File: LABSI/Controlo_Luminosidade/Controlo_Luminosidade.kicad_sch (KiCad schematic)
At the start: 43 parts, among them J1 Barrel_Jack_Switch, J10 Conn_01x03_Socket, J2 Barrel_Jack_Switch, J3 Conn_01x05_Pin, J4 Conn_01x04_Pin, J5 Conn_01x04_Pin, J6 AVR-ISP-6, J7 Conn_01x03_Pin, J8 Conn_01x03_Pin, J9 Conn_01x05_Pin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

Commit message: micro standalone, bug it reading lux sensors
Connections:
- net +5V: now also R1.2; no longer J6.5 (~{RST}), R1.1, U1.1 (~{RESET}/PC6)
- net GND: no longer R1.2
- net INT_PCF: no longer U1.14 (PB0)
- net at J10.2 (Pin_2), R8.2: no longer U3.11 (P6)
- new net RST-AVR: J6.5 (~{RST}), R1.1, U1.1 (~{RESET}/PC6)
- no-connect marks 8 -> 10
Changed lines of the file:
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@@
 	)
 	(junction
-		(at 116.84 45.72)
-		(diameter 0)
-		(color 0 0 0 0)
-	)
-	(junction
 		(at 233.68 92.71)
 		(diameter 0)
@@
 		(color 0 0 0 0)
 	)
-	(junction
-		(at 247.65 31.75)
-		(diameter 0)
-		(color 0 0 0 0)
-	)
 	(no_connect
 		(at 194.31 142.24)
@@
 	)
 	(no_connect
+		(at 194.31 81.28)
+	)
+	(no_connect
 		(at 194.31 106.68)
 	)
 	(no_connect
+		(at 104.14 45.72)
+	)
+	(no_connect
 		(at 194.31 134.62)
 	)
@@
 	(wire
 		(pts
-			(xy 247.65 31.75) (xy 248.92 31.75)
-		)
-		(stroke
-			(width 0)
-			(type default)
-		)
-	)
-	(wire
-		(pts
-			(xy 104.14 45.72) (xy 116.84 45.72)
-		)
-		(stroke
-			(width 0)
-			(type default)
-		)
-	)
-	(wire
-		(pts
 			(xy 195.58 20.32) (xy 203.2 20.32)
 		)
@@
 		)
 	)
-	(label "INT_PCF"
-		(at 194.31 81.28 0)
-		(effects
-			(font
-				(size 1.27 1.27)
-			)
-			(justify left bottom)
-		)
-	)
 	(label "XTAL1"
 		(at 259.08 59.69 0)
@@
 	(symbol
 		(lib_id "power:+5V")
-		(at 248.92 31.75 270)
+		(at 247.65 40.64 180)
 		(unit 1)
 		(exclude_from_sim no)
@@
 		(dnp no)
 		(property "Reference" "#PWR06"
-			(at 245.11 31.75 0)
+			(at 247.65 36.83 0)
 			(effects
 				(font
@@
 		)
 		(property "Value" "+5V"
-			(at 252.476 30.48 0)
+			(at 248.92 44.196 0)
 			(effects
 				(font
@@
 		)
 		(property "Footprint" ""
-			(at 248.92 31.75 0)
+			(at 247.65 40.64 0)
 			(effects
 				(font
@@
 		)
 		(property "Datasheet" ""
-			(at 248.92 31.75 0)
+			(at 247.65 40.64 0)
 			(effects
 				(font
@@
 		)
 		(property "Description" "Power symbol creates a global label with name \"+5V\""
-			(at 248.92 31.75 0)
+			(at 247.65 40.64 0)
 			(effects
 				(font
@@
 					(unit 1)
 				)
-			)
-		)
-	)
-	(symbol
-		(lib_id "power:GND")
-		(at 247.65 40.64 0)
-		(unit 1)
-		(exclude_from_sim no)
-		(in_bom yes)
-		(on_board yes)
-		(dnp no)
-		(property "Reference" "#PWR08"
-			(at 247.65 46.99 0)
-			(effects
-				(font
-					(size 1.27 1.27)
-				)
-				(hide yes)
-			)
-		)
-		(property "Value" "GND"
-			(at 246.126 44.196 0)
-			(effects
-				(font
-					(size 1.27 1.27)
-				)
-			)
-		)
-		(property "Footprint" ""
-			(at 247.65 40.64 0)
-			(effects
-				(font
-					(size 1.27 1.27)
-				)
-				(hide yes)
-			)
-		)
-		(property "Datasheet" ""
-			(at 247.65 40.64 0)
-			(effects
-				(font
-					(size 1.27 1.27)
-				)
-				(hide yes)
-			)
-		)
-		(property "Description" "Power symbol creates a global label with name \"GND\" , ground"
-			(at 247.65 40.64 0)
-			(effects
-				(font
-					(size 1.27 1.27)
-				)
-				(hide yes)
-			)
-		)
-		(pin "1"
-		)
-		(instances
-			(project "Controlo_Luminosidade"
-				(path "/fe63ea70-5567-4436-89bb-13eb6300ee5a"
-					(reference "#PWR08")
-					(unit 1)
-				)

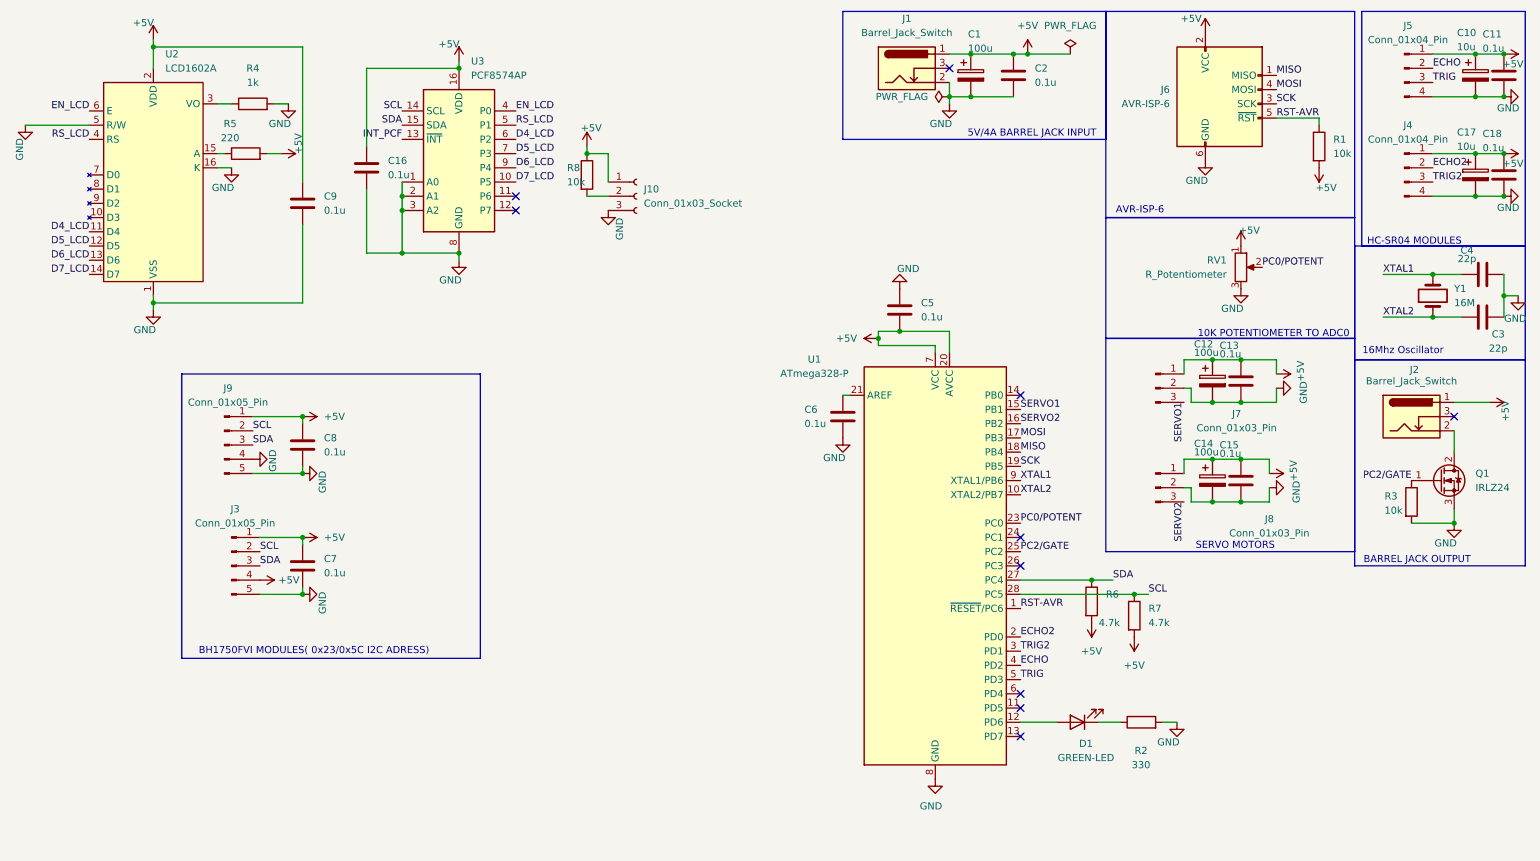
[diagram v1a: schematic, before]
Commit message: rotina maquina de estados inic; i2c, 2 sensors bug fixed, button logic added
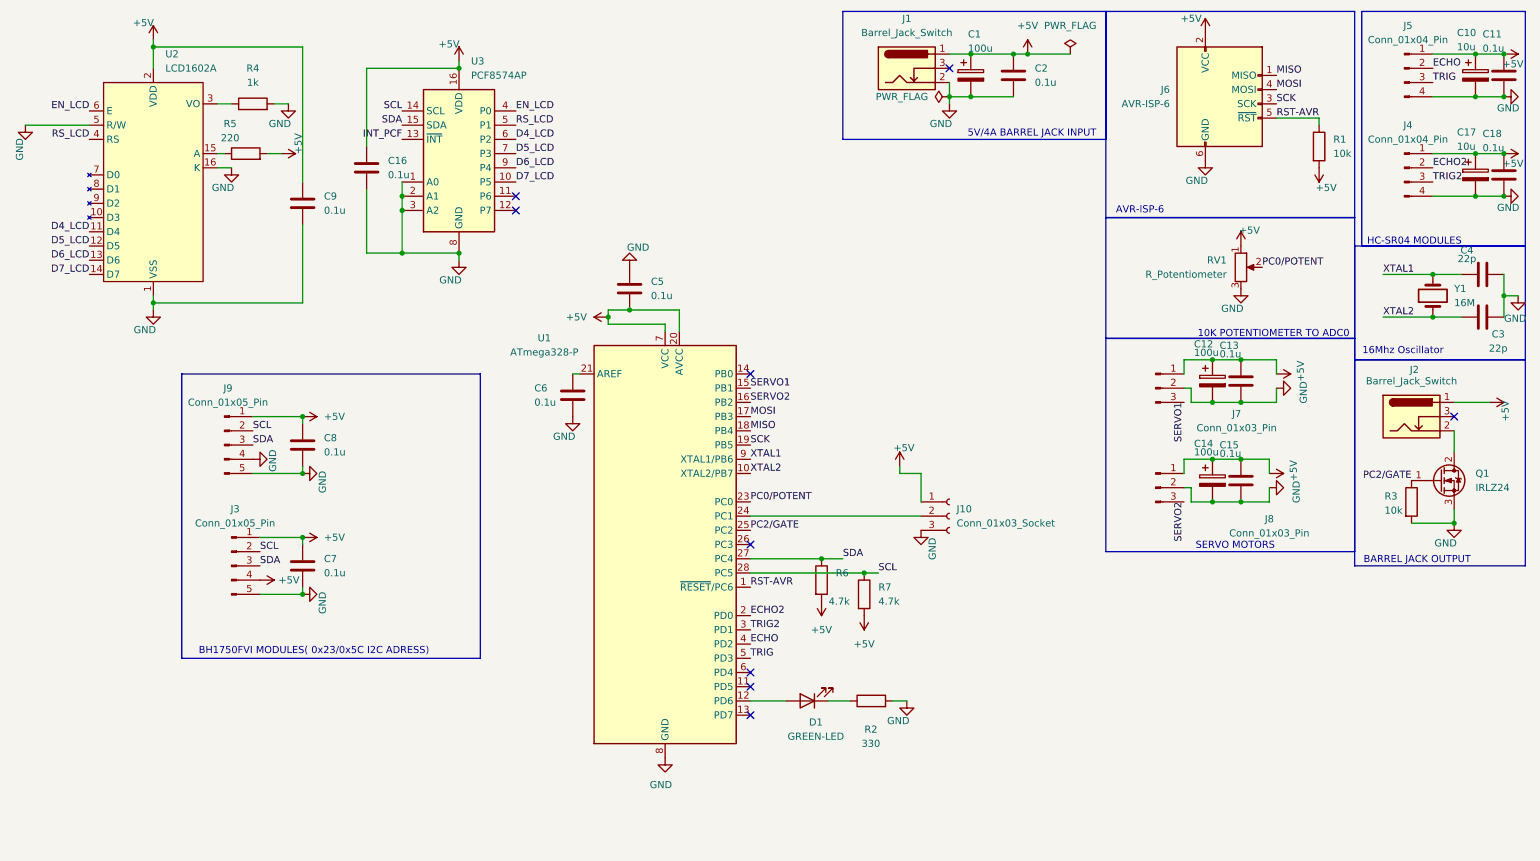
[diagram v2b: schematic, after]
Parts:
- removed R8: 10k, symbol Device:R
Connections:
- net at J10.2 (Pin_2): now also U1.24 (PC1)
- no-connect marks 10 -> 9
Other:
- moved on the sheet: C5, C6, D1, J10, R2, R6, R7, U1

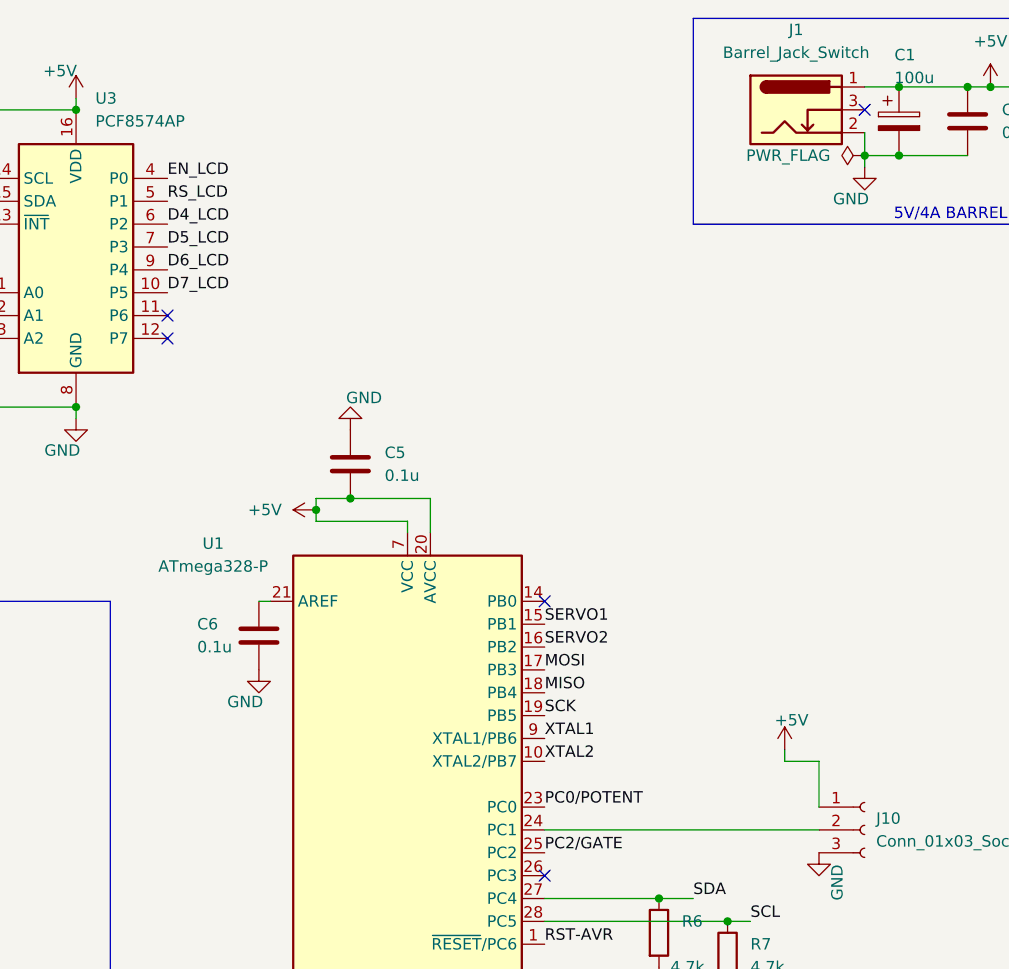
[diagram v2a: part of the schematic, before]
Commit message: maquina estados controlo adc, butao para modos, mapeamento para saltos de 50 e fixação setpoint
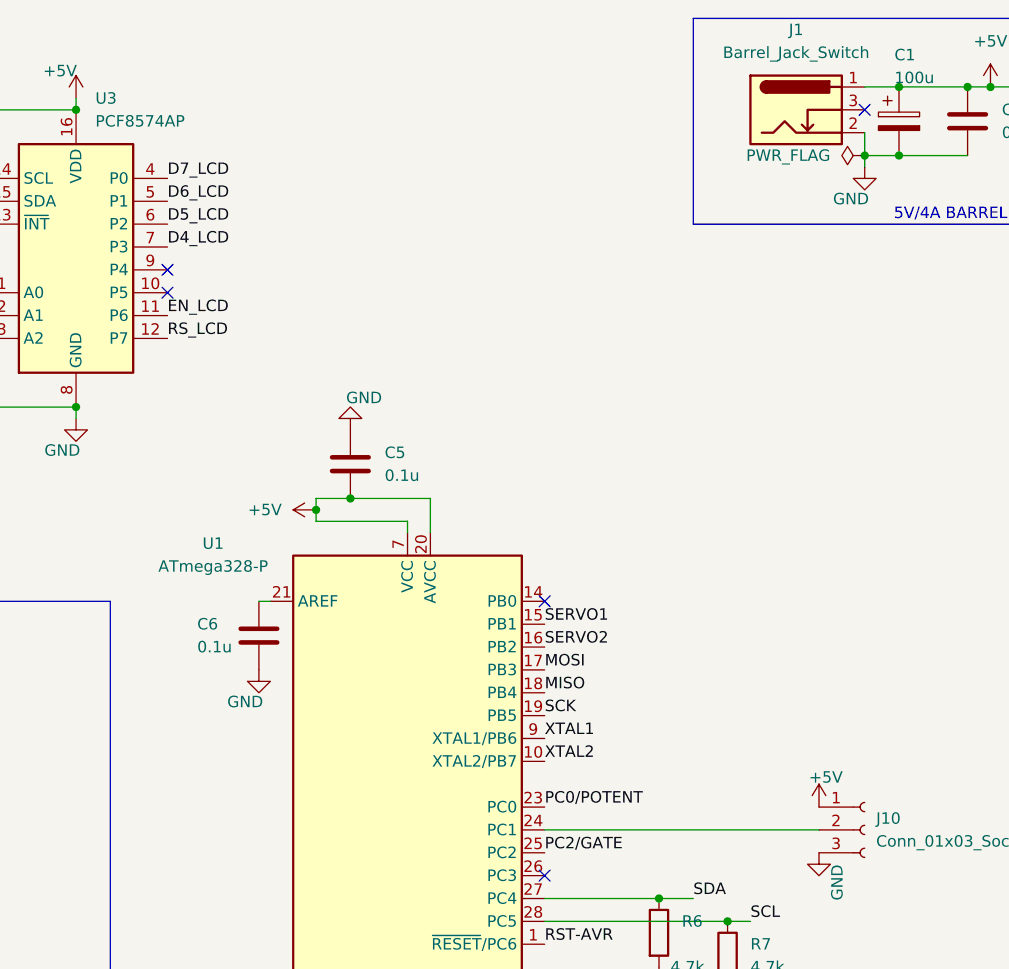
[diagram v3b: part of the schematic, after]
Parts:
- J10: footprint (none) -> Connector_PinSocket_2.54mm:PinSocket_1x03_P2.54mm_Vertical
- R6, R7: footprint (none) -> Resistor_THT:R_Axial_DIN0204_L3.6mm_D1.6mm_P5.08mm_Horizontal
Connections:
- net D4_LCD: now also U3.7 (P3); no longer U3.6 (P2)
- net D5_LCD: now also U3.6 (P2); no longer U3.7 (P3)
- net D6_LCD: now also U3.5 (P1); no longer U3.9 (P4)
- net D7_LCD: now also U3.4 (P0); no longer U3.10 (P5)
- net EN_LCD: now also U3.11 (P6); no longer U3.4 (P0)
- net RS_LCD: now also U3.12 (P7); no longer U3.5 (P1)
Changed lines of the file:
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@@
 	)
 	(no_connect
+		(at 104.14 40.64)
+	)
+	(no_connect
 		(at 146.05 138.43)
 	)
@@
 	)
 	(no_connect
-		(at 104.14 45.72)
+		(at 104.14 43.18)
 	)
 	(no_connect
@@
 	)
 	(no_connect
-		(at 104.14 48.26)
-	)
-	(no_connect
 		(at 146.05 107.95)
 	)
@@
 	(wire
 		(pts
-			(xy 172.72 95.25) (xy 176.53 95.25)
-		)
-		(stroke
-			(width 0)
-			(type default)
-		)
-	)
-	(wire
-		(pts
 			(xy 280.67 38.1) (xy 275.59 38.1)
 		)
@@
 	(wire
 		(pts
-			(xy 172.72 93.98) (xy 172.72 95.25)
-		)
-		(stroke
-			(width 0)
-			(type default)
-		)
-	)
-	(wire
-		(pts
 			(xy 224.79 82.55) (xy 228.6 82.55)
 		)
@@
 	(wire
 		(pts
-			(xy 176.53 95.25) (xy 176.53 100.33)
-		)
-		(stroke
-			(width 0)
-			(type default)
-		)
-	)
-	(wire
-		(pts
 			(xy 185.42 27.94) (xy 193.04 27.94)
 		)
@@
 	)
 	(label "D7_LCD"
-		(at 104.14 43.18 0)
+		(at 104.14 30.48 0)
 		(effects
 			(font
@@
 	)
 	(label "EN_LCD"
-		(at 104.14 30.48 0)
+		(at 104.14 45.72 0)
 		(effects
 			(font
@@
 	)
 	(label "D4_LCD"
-		(at 104.14 35.56 0)
+		(at 104.14 38.1 0)
 		(effects
 			(font
@@
 	)
 	(label "D5_LCD"
-		(at 104.14 38.1 0)
+		(at 104.14 35.56 0)
 		(effects
 			(font
@@
 	)
 	(label "D6_LCD"
-		(at 104.14 40.64 0)
+		(at 104.14 33.02 0)
 		(effects
 			(font
@@
 	)
 	(label "RS_LCD"
-		(at 104.14 33.02 0)
+		(at 104.14 48.26 0)
 		(effects
 			(font
@@
 			)
 		)
-		(property "Footprint" ""
+		(property "Footprint" "Resistor_THT:R_Axial_DIN0204_L3.6mm_D1.6mm_P5.08mm_Horizontal"
 			(at 156.972 114.3 90)
 			(effects
@@
 			)
 		)
-		(property "Footprint" ""
+		(property "Footprint" "Connector_PinSocket_2.54mm:PinSocket_1x03_P2.54mm_Vertical"
 			(at 181.61 102.87 0)
 			(effects
@@
 			)
 		)
-		(property "Footprint" ""
+		(property "Footprint" "Resistor_THT:R_Axial_DIN0204_L3.6mm_D1.6mm_P5.08mm_Horizontal"
 			(at 164.592 116.84 90)
 			(effects
@@
 	(symbol
 		(lib_id "power:+5V")
-		(at 172.72 93.98 0)
+		(at 176.53 100.33 0)
 		(unit 1)
 		(exclude_from_sim no)
@@
 		(dnp no)
 		(property "Reference" "#PWR042"
-			(at 172.72 97.79 0)
+			(at 176.53 104.14 0)
 			(effects
 				(font
@@
 		)
 		(property "Value" "+5V"
-			(at 173.482 90.678 0)
+			(at 177.292 97.028 0)
 			(effects
 				(font
@@
 		)
 		(property "Footprint" ""
-			(at 172.72 93.98 0)
+			(at 176.53 100.33 0)
 			(effects
 				(font
@@
 		)
 		(property "Datasheet" ""
-			(at 172.72 93.98 0)
+			(at 176.53 100.33 0)
 			(effects
 				(font
@@
 		)
 		(property "Description" "Power symbol creates a global label with name \"+5V\""
-			(at 172.72 93.98 0)
+			(at 176.53 100.33 0)
 			(effects
 				(font

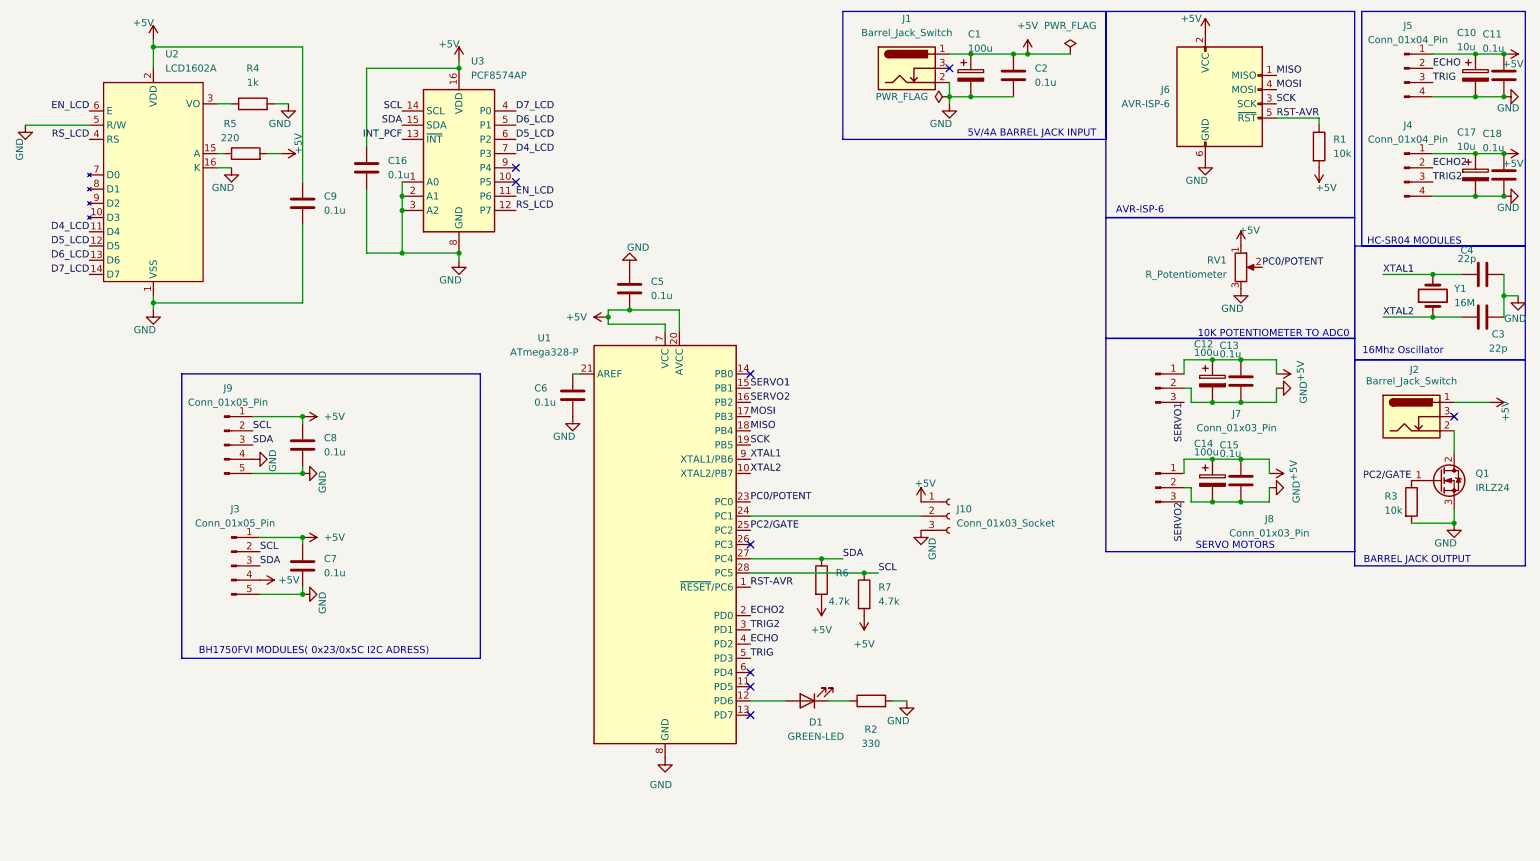
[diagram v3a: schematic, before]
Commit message: botoes para setpoint, buzzer adicionado, motor adicionado
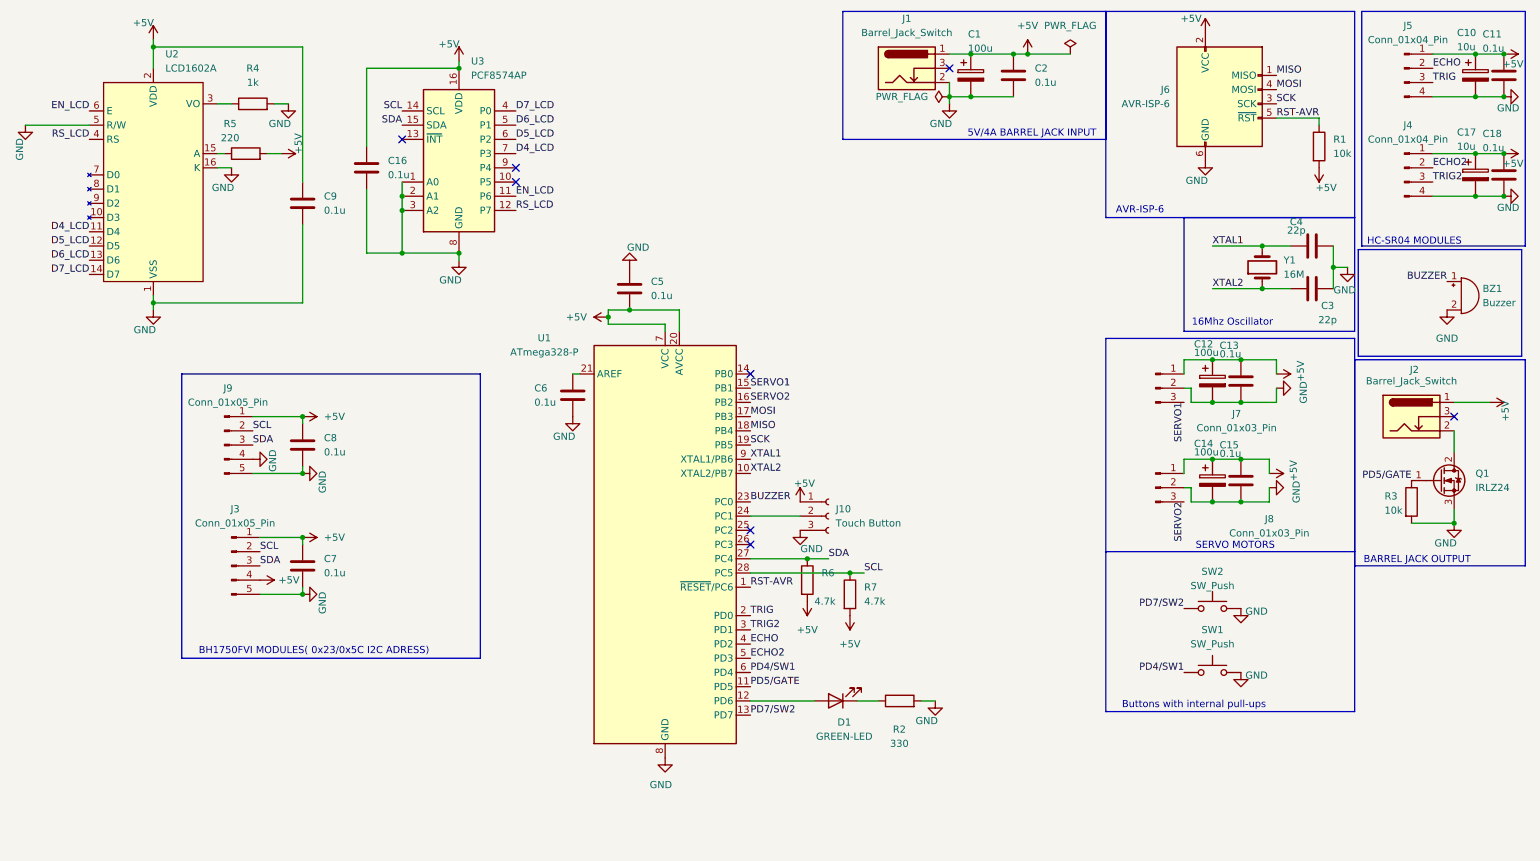
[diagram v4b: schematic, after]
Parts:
- removed RV1: R_Potentiometer, P160KN-0QC15B500K:P160, symbol Device:R_Potentiometer
- added BZ1: Buzzer, symbol Device:Buzzer
- added SW1, SW2: SW_Push, symbol Switch:SW_Push
- J10: value Conn_01x03_Socket -> Touch Button
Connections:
- net ECHO2: now also U1.5 (PD3); no longer U1.2 (PD0)
- net GND: now also BZ1.2 (-), SW1.2, SW2.2
- net TRIG: now also U1.2 (PD0); no longer U1.5 (PD3)
- net PD5/GATE: now reaches U1.11 (PD5)
- net PD5/GATE: now also Q1.1 (G), R3.1
- net PD7/SW2: now reaches U1.13 (PD7)
- net PD7/SW2: now also SW2.1
- net PD4/SW1: now reaches U1.6 (PD4)
- net PD4/SW1: now also SW1.1
- net INT_PCF: no longer names the net of U3.13 (~{INT})
- net PC0/POTENT renamed BUZZER
- net BUZZER: now also BZ1.1 (+)
- removed net PC2/GATE: Q1.1 (G), R3.1, U1.25 (PC2)
- no-connect marks 9 -> 8
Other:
- note added: "Buttons with internal pull-ups"
- note removed: "10K POTENTIOMETER TO ADC0"
- moved on the sheet: C3, C4, D1, J10, R2, R6, R7, Y1
